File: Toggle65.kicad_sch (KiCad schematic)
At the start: 163 parts, among them SW1 LatchMSB, SW10 SP3T, SW11 SP3T, SW12 RST, SW13 Write RAM, SW14 RAM or Toggle, SW15 SP3T, SW16 SP3T, SW17 SP3T, SW18 SP3T, SW19 SP3T, SW2 SP3T, SW20 SP3T, SW21 SP3T, SW22 SP3T, SW3 SP3T, SW4 SP3T, SW5 SP3T, SW6 SP3T, SW7 SP3T, SW8 SP3T, SW9 SP3T, U1 74LS573, U2 74HC74, U3 74HC00, U4 74HC245, U5 74HC245, U6 HM62256BLP, U7 R6507

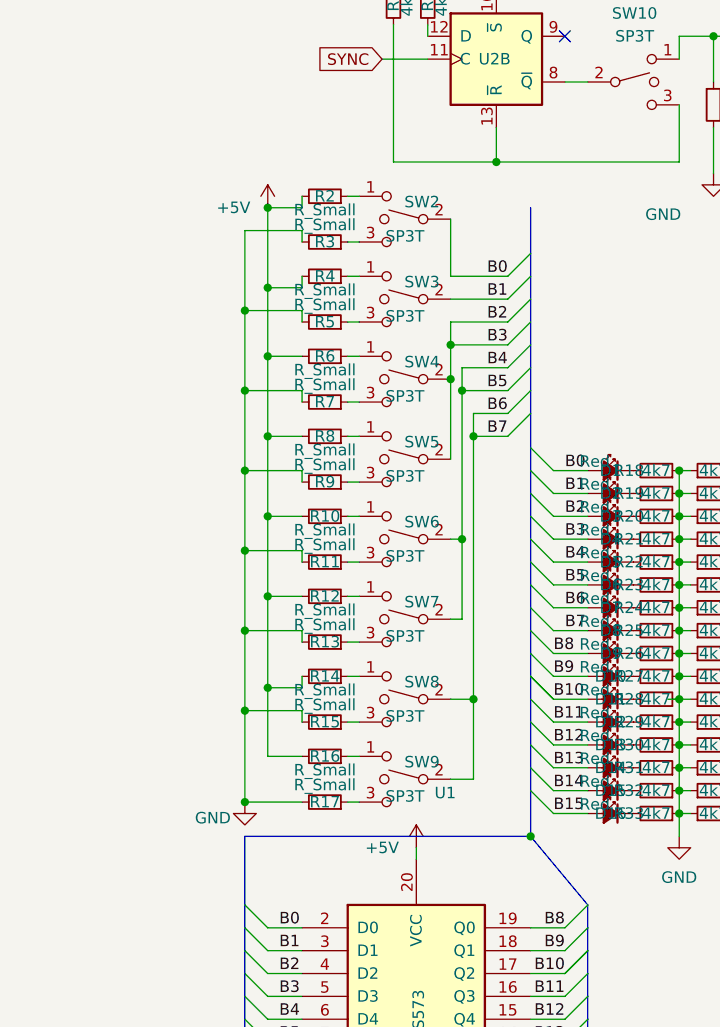
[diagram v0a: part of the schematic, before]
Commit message: fix: shorted addr switches
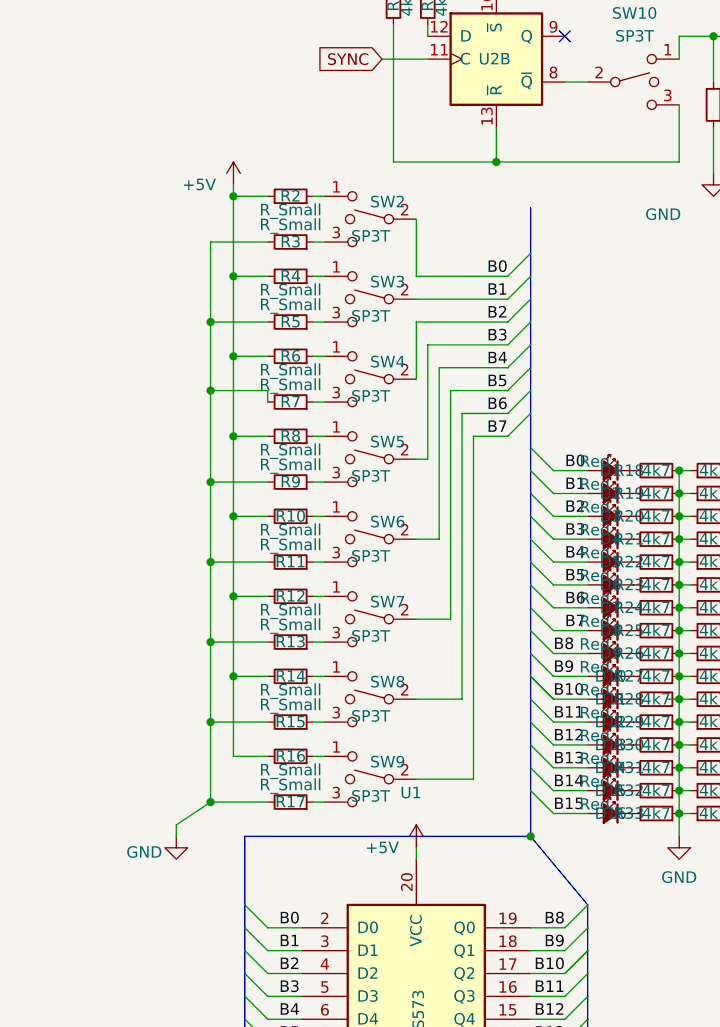
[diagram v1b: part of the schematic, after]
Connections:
- net B2: no longer D4.2 (A), SW5.2, U1.5 (D3), U4.15 (B3), U6.7 (A3)
- net B4: no longer D6.2 (A), SW7.2, U1.7 (D5), U4.13 (B5), U6.5 (A5)
- net B6: no longer D8.2 (A), SW9.2, U1.9 (D7), U4.11 (B7), U6.3 (A7)
- new net B3: D4.2 (A), SW5.2, U1.5 (D3), U4.15 (B3), U6.7 (A3)
- new net B5: D6.2 (A), SW7.2, U1.7 (D5), U4.13 (B5), U6.5 (A5)
- new net B7: D8.2 (A), SW9.2, U1.9 (D7), U4.11 (B7), U6.3 (A7)
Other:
- moved on the sheet: R10, R11, R12, R13, R14, R15, R16, R17, R2, R3, R4, R5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
